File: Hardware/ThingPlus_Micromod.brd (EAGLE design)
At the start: 91.4 x 22.9 mm, 151 parts, among them J4 QWIIC_RIGHT_ANGLE, J5 MICRO-SD-SDIOPUSH-PUSH, J6 JTAG, J7 MICROMOD-2222-C, U2 MCP73831, U3 MAX17048, U4 3.3V, U6 AP7361C-33

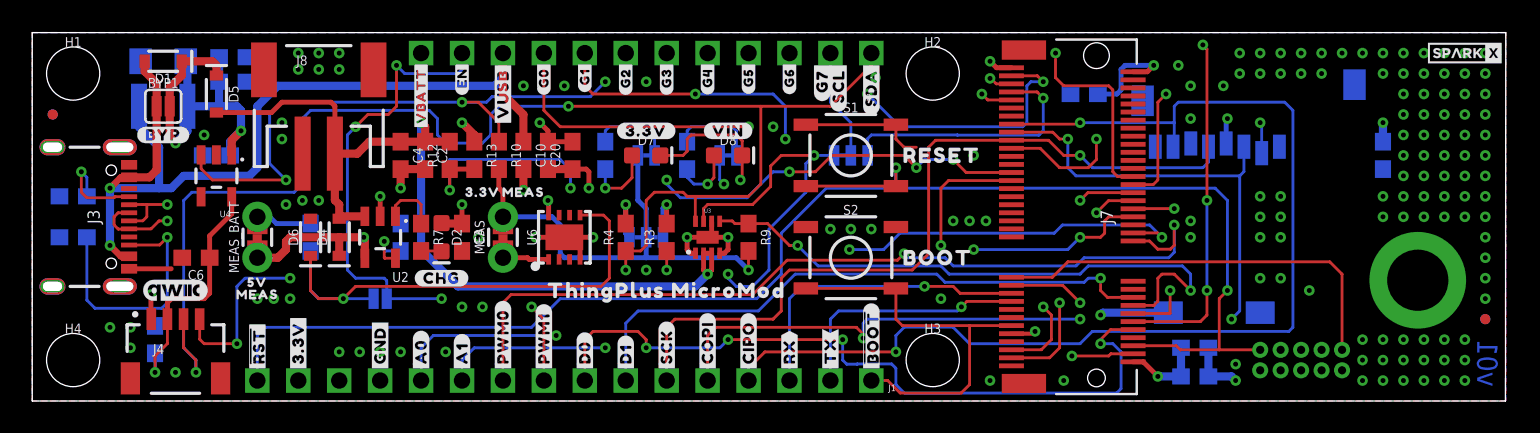
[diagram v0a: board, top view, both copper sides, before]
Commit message: Updated layout per Nathan's recommendations
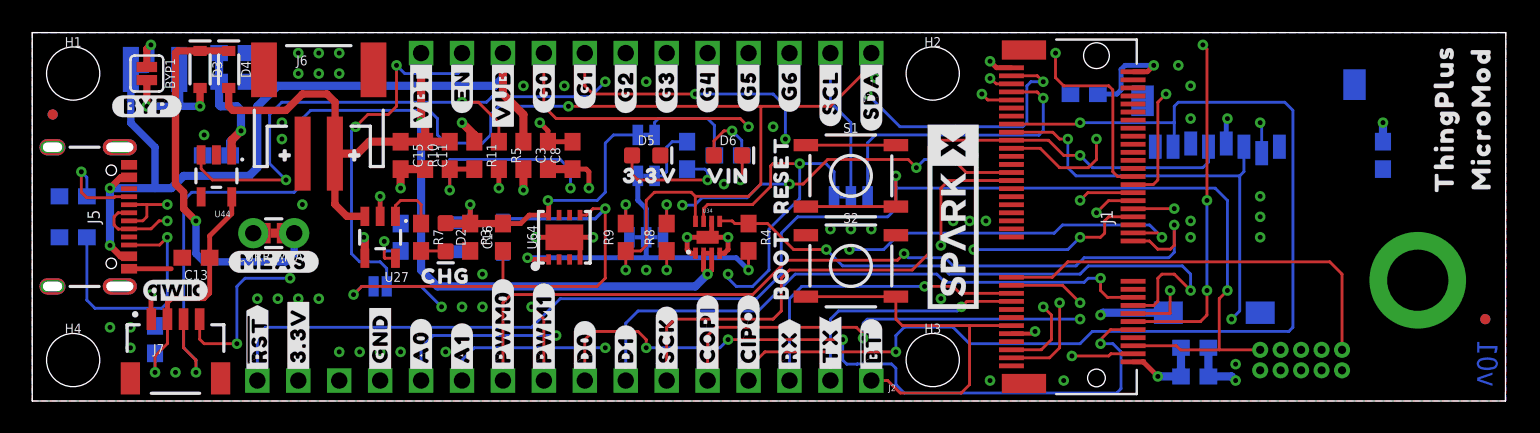
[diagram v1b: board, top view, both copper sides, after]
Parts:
- removed C17: 0.22uF, SparkFun-Capacitors:0603
- removed C18, C21: 0.1uF, SparkFun-Capacitors:0603
- removed C19: 10uF, SparkFun-Capacitors:EIA3216
- removed C20: 1.0uF, SparkFun-Capacitors:0603
- removed D7: RED, SparkFun-LED:LED-0603
- removed D8: Yellow, SparkFun-LED:LED-0603
- removed F2: 6V/2A, SparkFun-Fuses:1210
- removed JP4: JUMPER-SMT_3_1-NC_TRACE_SILK, SparkFun-Jumpers:SMT-JUMPER_3_1-NC_TRACE_SILK
- removed MEAS, MEAS_BATT: (no value), SparkFun-Jumpers:COMBO-JUMPER_2_NC_TRACE
- removed R15: 100k, SparkFun-Resistors:0603
- removed R16: 1k, SparkFun-Resistors:0603
- removed R17: 4.7k, SparkFun-Resistors:0603
- removed U$75, U$77: (no value), output:MEAS18
- removed U$76: (no value), output:5V18
- removed U$78: (no value), output:#SCL#G7#23
- removed U$79, U$80: (no value), output:THINGPLUS_MICROMOD25
- added C1, C14: 0.1uF, SparkFun-Capacitors:0603
- added C12: 1.0uF, SparkFun-Capacitors:0603
- added C15, C16: 4.7uF, SparkFun-Capacitors:0603
- added CURR_MEAS: (no value), SparkFun-Jumpers:COMBO-JUMPER_2_NC_TRACE
- added D3: 3A/10V/280mV, SparkFun-DiscreteSemi:SOD-323
- added F1: 6V/2A, SparkFun-Fuses:1210
- added R11: 10k, SparkFun-Resistors:0603
- added R5: 100k, SparkFun-Resistors:0603
- added R8: 2.2k, SparkFun-Resistors:0603
- added SCL/G7: JUMPER-SMT_3_1-NC_TRACE_SILK, SparkFun-Jumpers:SMT-JUMPER_3_1-NC_TRACE_SILK
- added U$69: (no value), output:#3#3V_LED#25
- C13, C2, C8: value 0.1uF -> 1.0uF
- C3, C4: value 4.7uF -> 0.1uF
- C5: value 1.0uF -> 10uF; device SparkFun-Capacitors:0603 -> SparkFun-Capacitors:0805
- C6: value 1.0uF -> 0.22uF
- C7: value 1.0uF -> 0.1uF
- D1: value 3A/10V/280mV -> 3.3V
- D5: value 3A/10V/280mV -> RED; device SparkFun-DiscreteSemi:SOD-323 -> SparkFun-LED:LED-0603
- D6: value 3.3V -> Yellow; device SparkFun-DiscreteSemi:SOD-323 -> SparkFun-LED:LED-0603
- J1: value (none) -> MICROMOD-2222-C; device SparkFun-Connectors:1X16_SM_SQ_NOSILK -> SparkFun-MicroMod:M.2-CONNECTOR-E
- J2: device SparkFun-Connectors:1X12_SM_SQ_NOSILK -> SparkFun-Connectors:1X16_SM_SQ_NOSILK
- J3: device SparkFun-Connectors:USB-C-16P_4LAYER-PADS -> SparkFun-Connectors:1X12_SM_SQ_NOSILK
- J4: value QWIIC_RIGHT_ANGLE -> MICRO-SD-SDIOPUSH-PUSH; device SparkFun-Connectors:JST04_1MM_RA -> SparkFun-Connectors:MICRO-SD-SOCKET
- J5: value MICRO-SD-SDIOPUSH-PUSH -> (none); device SparkFun-Connectors:MICRO-SD-SOCKET -> SparkFun-Connectors:USB-C-16P_4LAYER-PADS
- J6: value JTAG -> (none); device SparkFun-Connectors:2X5-PTH-1.27MM -> SparkFun-Connectors:JST-2-SMD
- J7: value MICROMOD-2222-C -> QWIIC_RIGHT_ANGLE; device SparkFun-MicroMod:M.2-CONNECTOR-E -> SparkFun-Connectors:JST04_1MM_RA
- J8: value (none) -> JTAG; device SparkFun-Connectors:JST-2-SMD -> SparkFun-Connectors:2X5-PTH-1.27MM
- LOGO1: value OSHW-LOGOS -> OSHW-LOGOMINI; device SparkFun-Aesthetics:OSHW-LOGO-S -> SparkFun-Aesthetics:OSHW-LOGO-MINI
- R10: value 100k -> 20k
- R12: value 20k -> 1k
- R13: value 10k -> 4.7k
- R3: value 2.2k -> 100k
- R4: value 2.2k -> 10k
- R9: value 10k -> 2.2k
- U$1: value SPARKX-LOGO2 -> SPARKX-LOGO5; device SparkX:SPARKX-TINY -> SparkX:SPARKX-LARGE
- U$10: device output:3#3V18 -> output:#D0#5
- U$11: device output:MEAS18 -> output:#PWM0#5
- U$12: device output:#CHG#18 -> output:#PWM1#5
- U$13: device output:5V18 -> output:#A1#5
- U$14: device output:MEAS18 -> output:#A0#5
- U$15: device output:#D0#5 -> output:#GND#4
- U$16: device output:#D1#5 -> output:#3#3V#1
- U$17: device output:#SCK#5 -> output:##RST##0
- U$18: device output:#COPI#6 -> output:#MEAS#25
- U$19: device output:#CIPO#7 -> output:CHG20
- U$2: value SPARKX-LOGO4 -> SPARKX-LOGO5; device SparkX:SPARKX-MEDIUM -> SparkX:SPARKX-LARGE
- U$20: device output:#RX#8 -> output:RESET19
- U$21: device output:#TX#9 -> output:BOOT18
- U$22: device output:##BOOT##10 -> output:#VBT#16
- U$23: device output:BOOT16 -> output:#EN#15
- U$24: device output:RESET17 -> output:#G0#14
- U$25: device output:#VBATT#13 -> output:#G1#14
- U$26: device output:#EN#13 -> output:#G2#14
- U$27: device output:#VUSB#13 -> output:#G3#14
- U$28: device output:#G0#12 -> output:#G4#14
- U$29: device output:#G1#12 -> output:#G5#14
- U$3: device output:##RST##0 -> output:##BT##11
- U$30: device output:#G2#12 -> output:#G6#14
- U$31: device output:#G3#12 -> output:#SCL#13
- U$32: device output:#G4#12 -> output:#SDA#12
- U$33: device output:#G5#12 -> output:3#3V22
- U$34: device output:#G6#12 -> output:VIN21
- U$35: device output:#SDA#11 -> output:#VUB#15
- U$36: device output:#G7#13 -> output:THINGPLUS29
- U$37: device output:#SCL#12 -> output:MICROMOD30
- U$38: device output:#VIN#21 -> output:#31
- U$39: device output:#3#3V#21 -> output:#32
- U$4, U$42: device output:#3#3V#1 -> output:#TX#9
- U$40: device output:#BYP#24 -> output:#BYP#27
- U$41: device output:##RST##0 -> output:#VE#16
- U$43, U$5: device output:#GND#4 -> output:#RX#8
- U$44, U$6: device output:#A0#5 -> output:#CIPO#7
- U$45, U$7: device output:#A1#5 -> output:#COPI#6
- U$46, U$8: device output:#PWM0#5 -> output:#SCK#5
- U$47, U$9: device output:#PWM1#5 -> output:#D1#5
- U$49: device output:#D1#5 -> output:#PWM0#5
- U$50: device output:#SCK#5 -> output:#PWM1#5
- U$51: device output:#COPI#6 -> output:#A1#5
- U$52: device output:#CIPO#7 -> output:#A0#5
- U$53: device output:#RX#8 -> output:#GND#4
- U$54: device output:#TX#9 -> output:#3#3V#1
- U$55: device output:##BOOT##10 -> output:##RST##0
- U$56: device output:#VBATT#13 -> output:##BOOT##10
- U$57: device output:#EN#13 -> output:#VBT#16
- U$58: device output:#VUSB#13 -> output:#EN#15
- U$59: device output:#G0#12 -> output:#G0#14
- U$60: device output:#G1#12 -> output:#G1#14
- U$61: device output:#G2#12 -> output:#G2#14
- U$62: device output:#G3#12 -> output:#G3#14
- U$63: device output:#G4#12 -> output:#G4#14
- U$64: device output:#G5#12 -> output:#G5#14
- U$65: device output:#G6#12 -> output:#G6#14
- U$66: device output:#SDA#11 -> output:#MEAS#25
- U$67: device output:#G7#13 -> output:#SDA#12
- U$68: device output:#SCL#12 -> output:#VUB#15
- U$70: device output:#3#3V_EN#22 -> output:#VIN_LED#25
- U$71: device output:#3#3V#21 -> output:#SCL#G7#14
- U$72: device output:#VIN#21 -> output:#I2C#27
- U$73: device output:#I2C#23 -> output:THINGPLUS_MICROMOD29
- U$74: device output:3#3V18 -> output:#SCL#G7#27
- moved C7 71.7 mm to (12.4, 21.6), turned to 180 degrees
- moved J6 63.2 mm to (17.8, 19.1), flipped to the top
- moved J8 63.2 mm to (78.7, 2.54), flipped to the bottom
- moved J5 62.4 mm to (6.35, 11.4), flipped to the top, turned to 270 degrees
- moved C13 62.4 mm to (10.2, 8.89), flipped to the top
- moved J4 59.6 mm to (68.5, 5.08), flipped to the bottom
- moved C2 59.4 mm to (83.8, 15.2), flipped to the bottom, turned to 90 degrees
- moved J7 57.5 mm to (8.89, 5.08), turned to 0 degrees
- moved C4 51.1 mm to (72.1, 1.52), flipped to the bottom, turned to 180 degrees
- moved J3 46.8 mm to (52.1, 21.6), turned to 180 degrees
- moved U$37 40.0 mm to (89.9, 17.5)
- moved U$36 38.8 mm to (87.6, 17.5)
- moved U$66 38.1 mm to (15.0, 12.2), turned to 0 degrees
- moved U$3 38.1 mm to (52.1, 1.65)
- moved U$55 38.1 mm to (14.0, 1.65)
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- renumbered C22 to C9, U2 to U27, U3 to U34, U4 to U44, U6 to U64
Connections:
- removed net 5V: C3.1, D2.A, D4.C, MEAS_BATT.1, MEAS_BATT.3, U27.4
- removed net N$1: MEAS.1, MEAS.3, U64.1
- new net N$2: JP1.3, R8.2
- new net N$5: CURR_MEAS.1, CURR_MEAS.3, D3.C, D4.C
- net !BOOT!: now also J1.11, J2.1; no longer J1.1, J7.11
- net !I2C_INT!: now also J1.16, R4.1; no longer J7.16, R9.1
- net !RST!: now also J1.6, J2.16, J8.10; no longer J1.16, J6.10, J7.6
- net !SD_CS!: now also J1.55, J4.CS/DAT3; no longer J5.CS/DAT3, J7.55
- net 3.3V: now also C1.2, C10.1, C2.2, C4.1, C8.1, J1.2, J1.74, J2.15, J4.VCC, J8.1, R4.2, R5.2, U64.1; no longer C13.1, C20.1, C21.1, C7.2, C8.2, J1.15, J5.VCC, J6.1, J7.2, J7.74, MEAS.2, MEAS.4, R10.2, R9.2
- net 3.3V_EN_VE: now also D1.C, R3.1; no longer D6.C, R15.1
- net A0: now also J1.34, J2.12; no longer J1.12, J7.34
- net A1: now also J1.38, J2.11; no longer J1.11, J7.38
- net BATT_VIN/3: now also J1.49, R10.1, R11.2; no longer J7.49, R12.1, R13.2
- net D0: now also J1.10, J2.8; no longer J1.8, J7.10
- net D1: now also J1.18, J2.7; no longer J1.7, J7.18
- net EN: now also J1.4, J3.11; no longer J2.11, J7.4
- net G0: now also J1.40, J3.9; no longer J2.9, J7.40
- net G1: now also J1.42, J3.8; no longer J2.8, J7.42
- net G2: now also J1.44, J3.7; no longer J2.7, J7.44
- net G3: now also J1.46, J3.6; no longer J2.6, J7.46
- net G4: now also J1.48, J3.5; no longer J2.5, J7.48
- net G5: now also J1.73, J3.4; no longer J2.4, J7.73
- net G6: now also J1.71, J3.3; no longer J2.3, J7.71
- net G7: now also J1.69, SCL/G7.1; no longer J7.69, JP4.1
- net GND: now also C1.1, C12.2, C14.2, C15.2, C16.2, C2.1, C7.2, C8.2, D1.A, D5.C, D6.C, J1.1, J1.33, J1.36, J1.39, J1.45, J1.7, J1.75, J2.13, J4.CD1, J4.GND, J4.GND1, J4.GND3, J5.GND2, J5.SHLD1, J5.SHLD2, J5.SHLD3, J5.SHLD4, J6.1, J8.3, J8.5, J8.9, R11.1; no longer C17.2, C18.2, C19.-, C2.2, C20.2, C21.2, C7.1, C8.1, D6.A, D7.C, D8.C, J1.13, J3.GND, J3.GND2, J3.SHLD1, J3.SHLD2, J3.SHLD3, J3.SHLD4, J4.1, J5.CD1, J5.GND1, J5.GND3, J6.3, J6.5, J6.9, J7.33, J7.36, J7.39, J7.45, J7.7, J7.75, J8.1, R13.1
- net N$10: now also R13.2; no longer R17.2
- net N$11: now also D6.A, R13.1; no longer D8.A, R17.1
- net N$12: now also J5.A5; no longer J3.A5
- net N$13: now also J5.B5; no longer J3.B5
- net N$3: now also JP1.1, R9.2; no longer JP1.3, R3.2
- net N$4: now also BYP1.2, D3.A, F1.2; no longer JP1.1, R4.2
- net N$6: now also R12.2; no longer R16.2
- net N$9: now also D5.A, R12.1; no longer D7.A, R16.1
- net PWM0: now also J1.32, J2.10; no longer J1.10, J7.32
- net PWM1: now also J1.47, J2.9; no longer J1.9, J7.47
- net QWIIC_EN: now also J1.67, R5.1; no longer J7.67, R10.1
- net QWIIC_PWR: now also C13.1, C14.1, J7.2; no longer C11.1, C6.1, J4.2
- net SCL: now also J1.14, J7.4, R8.1, SCL/G7.3; no longer J4.4, J7.14, JP4.3, R3.1
- net SCL/G7: now also J3.2, SCL/G7.2; no longer J2.2, JP4.2
- net SDA: now also J1.12, J3.1, J7.3, R9.1; no longer J2.1, J4.3, J7.12, R4.1
- net SPI_CIPO: now also J1.61, J2.4, J4.DO/DAT0; no longer J1.4, J5.DO/DAT0, J7.61
- net SPI_COPI: now also J1.59, J2.5, J4.DI/CMD; no longer J1.5, J5.DI/CMD, J7.59
- net SPI_SCK: now also J1.57, J2.6, J4.SCLK; no longer J1.6, J5.SCLK, J7.57
- net SWDCK: now also J1.21, J8.4; no longer J6.4, J7.21
- net SWDIO: now also J1.23, J8.2; no longer J6.2, J7.23
- net UART_RX: now also J1.19, J2.3; no longer J1.3, J7.19
- net UART_TX: now also J1.17, J2.2; no longer J1.2, J7.17
- net USB_D+: now also J1.3, J5.A6, J5.B6; no longer J3.A6, J3.B6, J7.3
- net USB_D-: now also J1.5, J5.A7, J5.B7; no longer J3.A7, J3.B7, J7.5
- net VIN: now also C12.1, C16.1, C6.1, C7.1, CURR_MEAS.2, CURR_MEAS.4, D2.A, R3.2, U27.4; no longer BYP1.2, C17.1, C18.1, C19.+, D1.C, D5.C, F2.2, MEAS_BATT.2, MEAS_BATT.4, R15.2
- net V_BATT: now also C11.1, C15.1, J3.12, J6.2, R10.2; no longer C2.1, C4.1, D5.A, J2.12, J8.2, R12.2
- net V_USB: now also C3.1, F1.1, J1.9, J3.10, J5.VBUS1, J5.VBUS2; no longer C10.1, D1.A, F2.1, J2.10, J3.VBUS1, J3.VBUS2, J7.9
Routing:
- net N$5: track 0.00 -> 24.9 mm, vias 0 -> 1
- net 5V: track 21.0 -> 0.00 mm, vias 2 -> 0
- net GND: track 50.8 -> 41.9 mm, vias 154 -> 63
- net VIN: track 67.1 -> 73.9 mm, vias 4 -> 5
- net 3.3V: track 47.2 -> 41.0 mm, vias 6 -> 8
- net N$4: track 3.31 -> 8.36 mm, vias 1 -> 2
- net N$1: track 3.64 -> 0.00 mm
- net N$9: track 4.50 -> 7.84 mm
- net N$2: track 0.00 -> 3.31 mm, vias 0 -> 1
- net V_USB: track 120.6 -> 117.7 mm, vias 3 -> 4
- net SCL/G7: track 6.88 -> 9.42 mm
- net G7: track 16.3 -> 18.7 mm
- net N$6: track 5.46 -> 3.79 mm
- net SCL: track 95.9 -> 97.2 mm
- net V_BATT: track 59.7 -> 61.0 mm
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
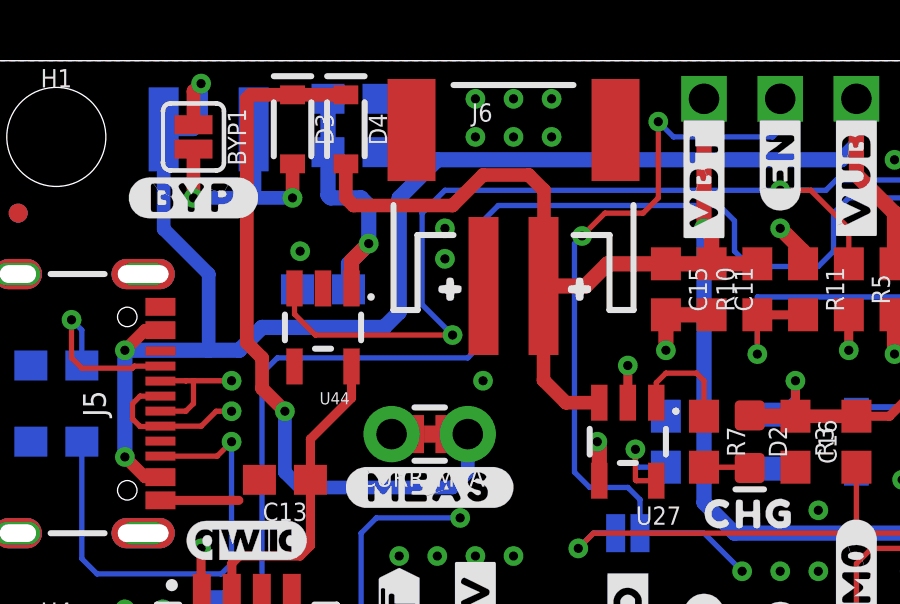
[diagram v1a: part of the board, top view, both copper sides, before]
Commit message: Fixed wrong battery polarity in top silk; panelized design
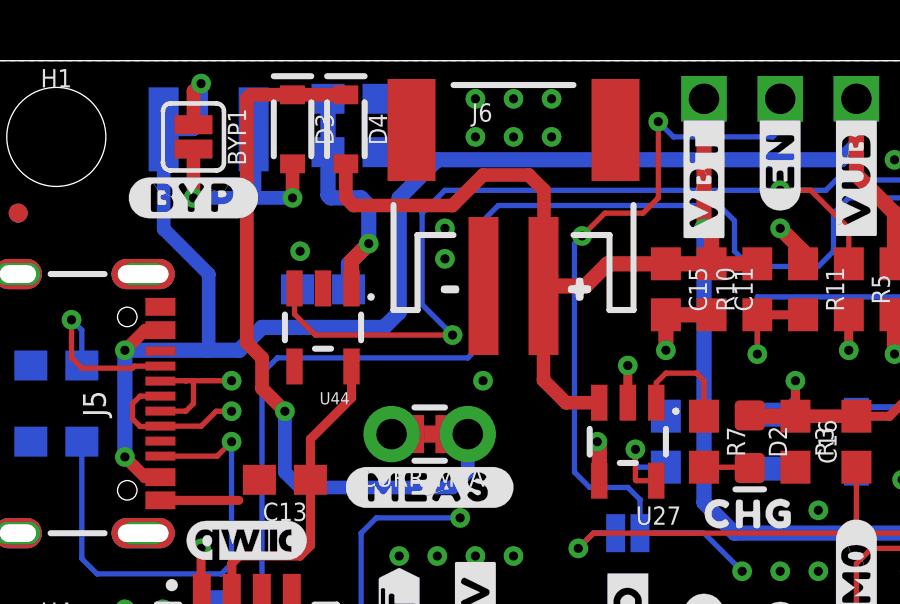
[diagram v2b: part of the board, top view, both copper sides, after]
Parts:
- U$39: device output:#32 -> output:#33
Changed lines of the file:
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@@
 <drawing>
 <settings>
-<setting alwaysvectorfont="yes"/>
+<setting alwaysvectorfont="no"/>
 <setting verticaltext="up"/>
 </settings>
-<grid distance="10" unitdist="mil" unit="mil" style="lines" multiple="1" display="yes" altdistance="0.005" altunitdist="inch" altunit="mil"/>
+<grid distance="0.05" unitdist="inch" unit="inch" style="lines" multiple="1" display="yes" altdistance="0.005" altunitdist="inch" altunit="inch"/>
 <layers>
 <layer number="1" name="Top" color="4" fill="1" visible="yes" active="yes"/>
@@
 <layer number="23" name="tOrigins" color="15" fill="1" visible="yes" active="yes"/>
 <layer number="24" name="bOrigins" color="15" fill="1" visible="yes" active="yes"/>
-<layer number="25" name="tNames" color="7" fill="1" visible="yes" active="yes"/>
-<layer number="26" name="bNames" color="7" fill="1" visible="yes" active="yes"/>
+<layer number="25" name="tNames" color="7" fill="1" visible="no" active="yes"/>
+<layer number="26" name="bNames" color="7" fill="1" visible="no" active="yes"/>
 <layer number="27" name="tValues" color="7" fill="1" visible="no" active="yes"/>
 <layer number="28" name="bValues" color="7" fill="1" visible="no" active="yes"/>
@@
 <layer number="37" name="tTest" color="7" fill="1" visible="no" active="yes"/>
 <layer number="38" name="bTest" color="7" fill="1" visible="no" active="yes"/>
-<layer number="39" name="tKeepout" color="4" fill="11" visible="yes" active="yes"/>
-<layer number="40" name="bKeepout" color="1" fill="11" visible="yes" active="yes"/>
+<layer number="39" name="tKeepout" color="4" fill="11" visible="no" active="yes"/>
+<layer number="40" name="bKeepout" color="1" fill="11" visible="no" active="yes"/>
 <layer number="41" name="tRestrict" color="4" fill="10" visible="no" active="yes"/>
 <layer number="42" name="bRestrict" color="1" fill="10" visible="no" active="yes"/>
@@
 <layer number="45" name="Holes" color="7" fill="1" visible="yes" active="yes"/>
 <layer number="46" name="Milling" color="3" fill="1" visible="no" active="yes"/>
-<layer number="47" name="Measures" color="7" fill="1" visible="yes" active="yes"/>
+<layer number="47" name="Measures" color="7" fill="1" visible="no" active="yes"/>
 <layer number="48" name="Document" color="7" fill="1" visible="no" active="yes"/>
 <layer number="49" name="Reference" color="7" fill="1" visible="no" active="yes"/>
@@
 <element name="U$37" library="output" package="MICROMOD30" value="" x="89.916" y="17.526" smashed="yes" rot="R90"/>
 <element name="U$38" library="output" package="#31" value="" x="20.066" y="15.24" smashed="yes"/>
-<element name="U$39" library="output" package="#32" value="" x="15.748" y="15.24" smashed="yes"/>
 <element name="U$40" library="output" package="#BYP#27" value="" x="7.112" y="18.288" smashed="yes"/>
 <element name="U$42" library="output" package="#TX#9" value="" x="49.53" y="1.651" smashed="yes" rot="MR90"/>
@@
 <element name="U$73" library="output" package="THINGPLUS_MICROMOD29" value="" x="57.15" y="9.398" smashed="yes" rot="MR0"/>
 <element name="U$41" library="output" package="#VE#16" value="" x="22.352" y="7.112" smashed="yes" rot="MR0"/>
+<element name="U$39" library="output" package="#33" value="" x="15.748" y="15.24" smashed="yes"/>
 </elements>
 <signals>
